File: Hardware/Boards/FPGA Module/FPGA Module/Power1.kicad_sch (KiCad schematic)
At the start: 0 parts

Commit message: FPGA Module schematic and part edits
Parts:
- added U2: LM7805MPX/NOPB, Package_TO_SOT_SMD:SOT-223-3_TabPin2, symbol DICE_FPGA_Module:LM7805MPX/NOPB
- added U3: AOZ2369QI-11, DICE_FPGA_Module:AOZ2369QI11, symbol DICE_FPGA_Module:AOZ2369QI-11
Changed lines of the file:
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@@
 	(generator "eeschema")
 	(generator_version "8.0")
-	(paper "A4")
+	(paper "A3")
 	(title_block
 		(title "Power1")
@@
 		(comment 1 "Designed by Michael Haahr")
 	)
+	(symbol
+		(lib_id "DICE_FPGA_Module:LM7805MPX/NOPB")
+		(at 63.5 118.11 0)
+		(unit 1)
+		(exclude_from_sim no)
+		(in_bom yes)
+		(on_board yes)
+		(dnp no)
+		(fields_autoplaced yes)
+		(property "Reference" "U2"
+			(at 63.5 109.22 0)
+			(effects
+				(font
+					(size 1.27 1.27)
+				)
+			)
+		)
+		(property "Value" "LM7805MPX/NOPB"
+			(at 63.5 111.76 0)
+			(effects
+				(font
+					(size 1.27 1.27)
+				)
+			)
+		)
+		(property "Footprint" "Package_TO_SOT_SMD:SOT-223-3_TabPin2"
+			(at 63.5 118.11 0)
+			(effects
+				(font
+					(size 1.27 1.27)
+				)
+				(hide yes)
+			)
+		)
+		(property "Datasheet" "https://ti.com/lit/ds/symlink/lm7800.pdf"
+			(at 63.5 118.11 0)
+			(effects
+				(font
+					(size 1.27 1.27)
+				)
+				(hide yes)
+			)
+		)
+		(property "Description" "Wide VIN 1.5-A 5V Regulator"
+			(at 63.5 118.11 0)
+			(effects
+				(font
+					(size 1.27 1.27)
+				)
+				(hide yes)
+			)
+		)
+		(pin "2"
+		)
+		(pin "3"
+		)
+		(pin "1"
+		)
+		(instances
+			(project ""
+				(path "/199f10e2-d4b4-4a27-9e84-7b1ce2ae6bf0/0c296310-f788-47f0-8a3f-43c3444563e8/e751a632-5f45-4f29-8d0a-1f9649251d32"
+					(reference "U2")
+					(unit 1)
+				)
+			)
+		)
+	)
+	(symbol
+		(lib_id "DICE_FPGA_Module:AOZ2369QI-11")
+		(at 63.5 63.5 0)
+		(unit 1)
+		(exclude_from_sim no)
+		(in_bom yes)
+		(on_board yes)
+		(dnp no)
+		(fields_autoplaced yes)
+		(property "Reference" "U3"
+			(at 63.5 27.94 0)
+			(effects
+				(font
+					(size 1.27 1.27)
+				)
+			)
+		)
+		(property "Value" "AOZ2369QI-11"
+			(at 63.5 30.48 0)
+			(effects
+				(font
+					(size 1.27 1.27)
+				)
+			)
+		)
+		(property "Footprint" "DICE_FPGA_Module:AOZ2369QI11"
+			(at 63.5 58.42 0)
+			(effects
+				(font
+					(size 1.27 1.27)
+				)
+				(hide yes)
+			)
+		)
+		(property "Datasheet" "https://www.aosmd.com/res/datasheets/AOZ2369QI-11.pdf"
+			(at 63.5 63.5 0)
+			(effects
+				(font
+					(size 1.27 1.27)
+				)
+				(hide yes)
+			)
+		)
+		(property "Description" "24V/30A Synchronous EZBuck Regulator"
+			(at 63.5 63.5 0)
+			(effects
+				(font
+					(size 1.27 1.27)
+				)
+				(hide yes)
+			)
+		)
+		(pin "14"
+		)
+		(pin "22"
+		)
+		(pin "25"
+		)
+		(pin "6"
+		)
+		(pin "7"
+		)
+		(pin "8"
+		)
+		(pin "11"
+		)
+		(pin "19"
+		)
+		(pin "5"
+		)
+		(pin "21"
+		)
+		(pin "18"
+		)
+		(pin "24"
+		)
+		(pin "27"
+		)
+		(pin "12"
+		)
+		(pin "13"
+		)
+		(pin "17"
+		)
+		(pin "15"
+		)
+		(pin "26"
+		)
+		(pin "28"
+		)
+		(pin "16"
+		)
+		(pin "3"
+		)
+		(pin "20"
+		)
+		(pin "23"
+		)
+		(pin "1"
+		)
+		(pin "10"
+		)
+		(pin "2"
+		)
+		(pin "4"
+		)
+		(pin "9"
+		)
+		(instances
+			(project ""
+				(path "/199f10e2-d4b4-4a27-9e84-7b1ce2ae6bf0/0c296310-f788-47f0-8a3f-43c3444563e8/e751a632-5f45-4f29-8d0a-1f9649251d32"
+					(reference "U3")
+					(unit 1)
+				)
+			)
+		)
+	)
 )

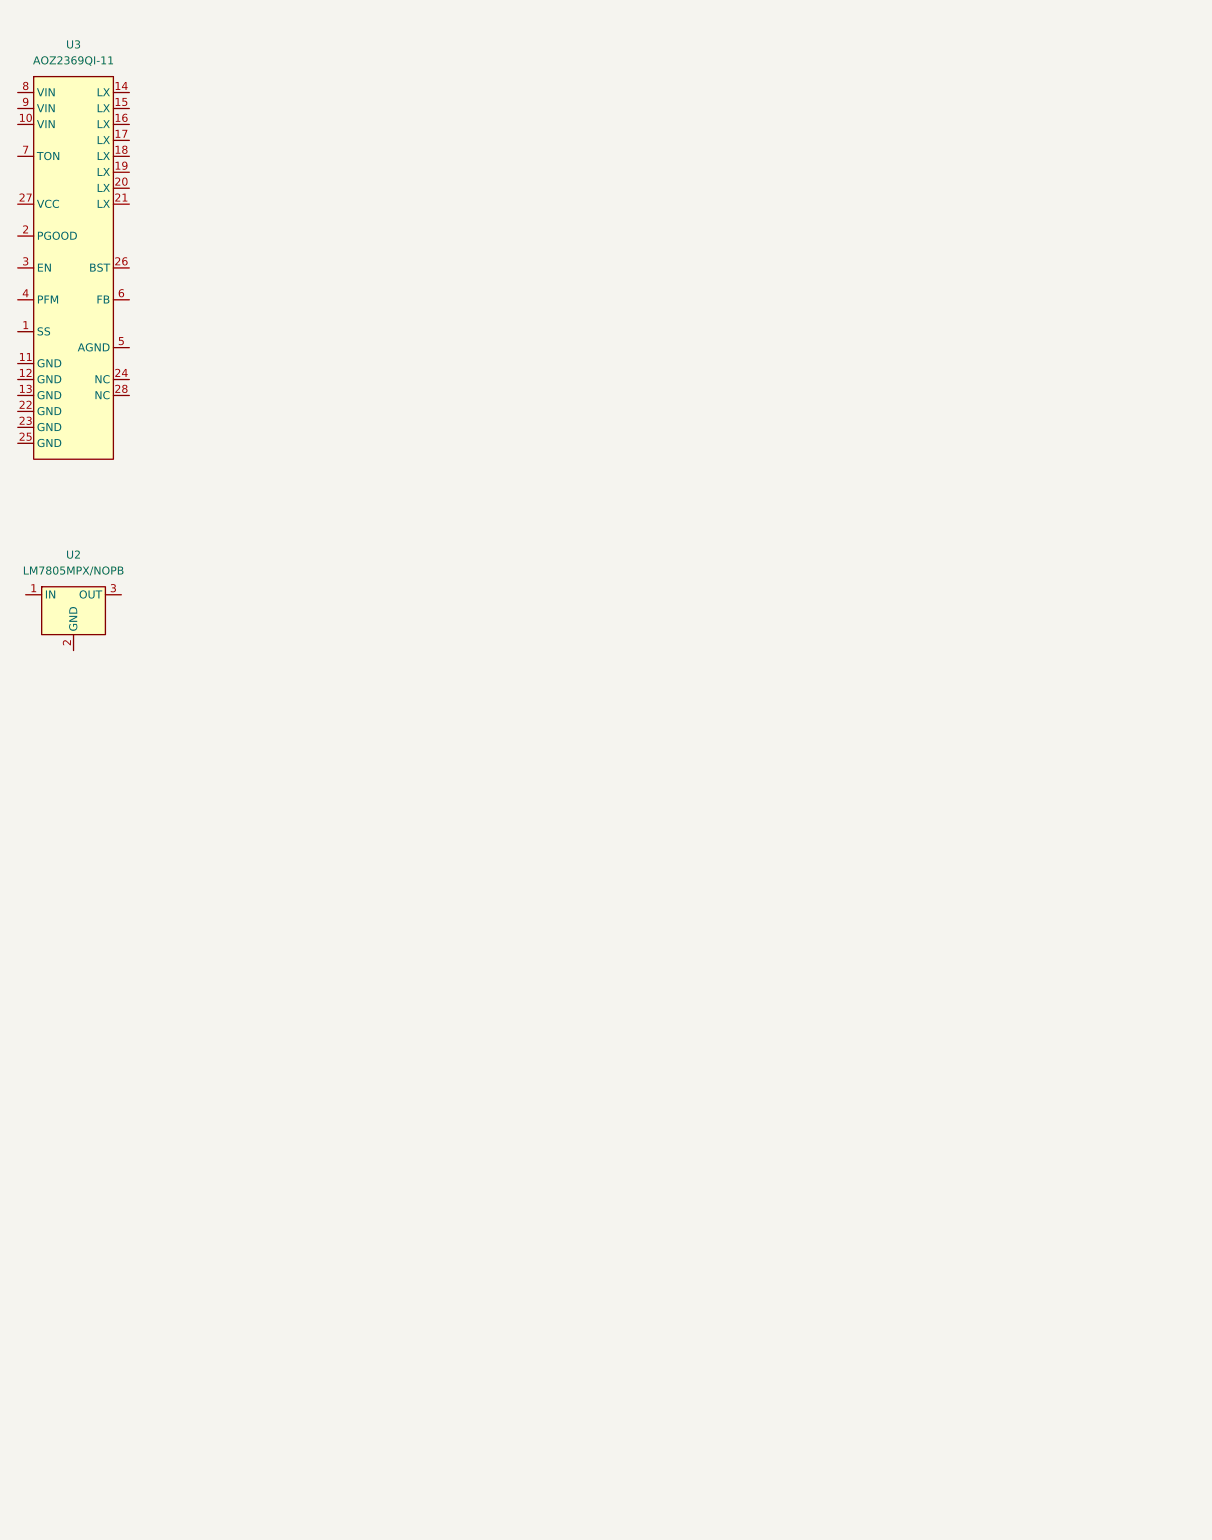
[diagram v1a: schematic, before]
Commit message: FPGA Board schematic work
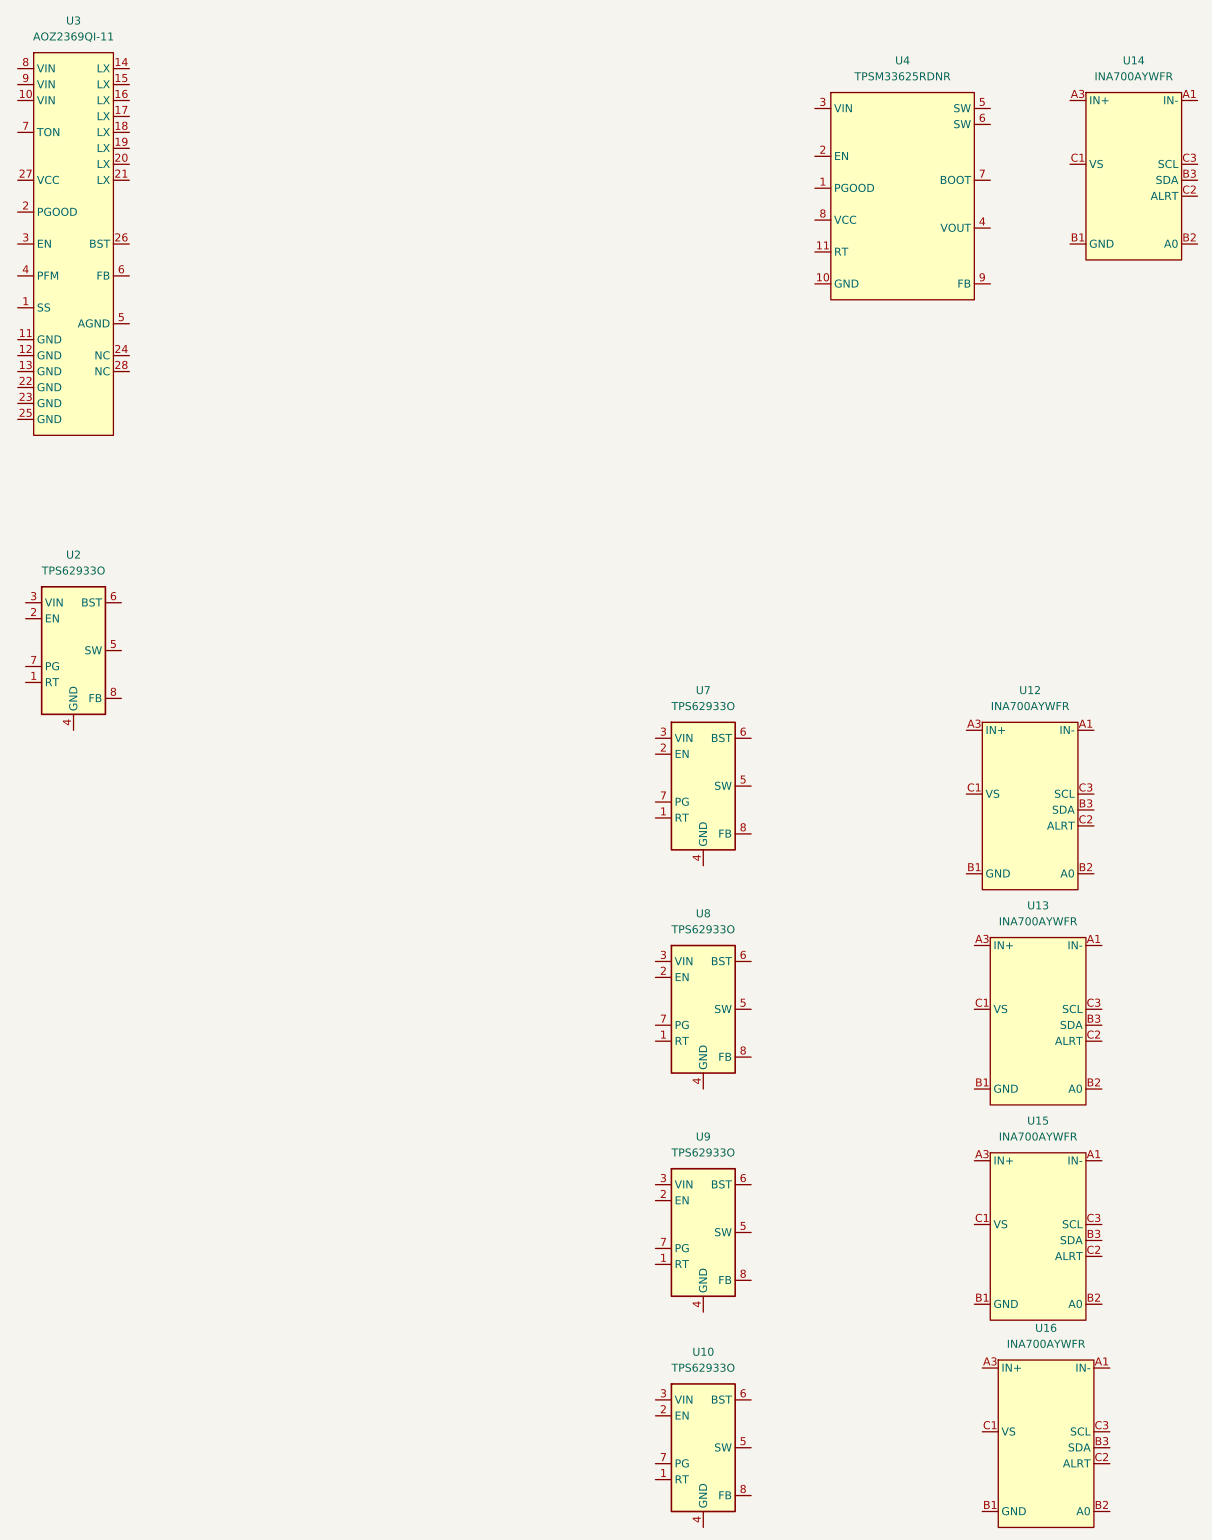
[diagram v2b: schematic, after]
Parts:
- removed U2: LM7805MPX/NOPB, Package_TO_SOT_SMD:SOT-223-3_TabPin2, symbol DICE_FPGA_Module:LM7805MPX/NOPB
- added U10, U2, U7, U8, U9: TPS62933O, Package_TO_SOT_SMD:SOT-583-8, symbol Regulator_Switching:TPS62933O
- added U12, U13, U14, U15, U16: INA700AYWFR, FPGA Module:INA700_AYWFR, symbol FPGA Module:INA700
- added U4: TPSM33625RDNR, FPGA Module:RDN0011A-MFG, symbol FPGA Module:TPSM33625
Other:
- moved on the sheet: U3

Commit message: FPGA Module Schematic work
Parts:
- removed U3: AOZ2369QI-11, DICE_FPGA_Module:AOZ2369QI11, symbol DICE_FPGA_Module:AOZ2369QI-11
- added C13, C17, C21, C23, C24: 100nF, Capacitor_SMD:C_0402_1005Metric, symbol Device:C_Small
- added C14, C15, C16: 100uF, Capacitor_SMD:C_0805_2012Metric, symbol Device:C_Small
- added C18: 4.7uF, Capacitor_SMD:C_0402_1005Metric, symbol Device:C_Small
- added C19, C20: 22uF, Capacitor_SMD:C_0805_2012Metric, symbol Device:C_Small
- added C22: 10uF, Capacitor_SMD:C_0603_1608Metric, symbol Device:C_Small
- added C25: 47uF, Capacitor_SMD:C_0603_1608Metric, symbol Device:C_Small
- added D2: LED, LED_SMD:LED_0603_1608Metric, symbol Device:LED
- added L1: 0.47uH, FPGA Module:INDM135125X500N, symbol Device:L
- added L2: 6.8uH, symbol Device:L
- added R10, R7, R8, R9: 3.3k, Resistor_SMD:R_0402_1005Metric, symbol Device:R_US
- added R11, R12: 33R, Resistor_SMD:R_0402_1005Metric, symbol Device:R_US
- added R13: 52.3k, Resistor_SMD:R_0402_1005Metric, symbol Device:R_US
- added R14: 9.09k, Resistor_SMD:R_0402_1005Metric, symbol Device:R_US
- added R15: 10k, Resistor_SMD:R_0402_1005Metric, symbol Device:R_US
- added R3: 100k, Resistor_SMD:R_0402_1005Metric, symbol Device:R_US
- added R4: 240k, Resistor_SMD:R_0402_1005Metric, symbol Device:R_US
- added R5: 67.3k, Resistor_SMD:R_0402_1005Metric, symbol Device:R_US
- added R6: 1mOhm, Resistor_SMD:R_1206_3216Metric, symbol Device:R_US
- added U18: INA236, Package_TO_SOT_SMD:SOT-23-8, symbol FPGA Module:INA236
- added U3: AOZ2369QI-11, FPGA Module:AOZ2369QI11, symbol FPGA Module:AOZ2369QI-11
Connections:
- net PP_VUSB: now reaches U2.3 (VIN)
- net PP_VUSB: now also C19.1, C20.1, C22.1, C23.1, R5.1, U3.10 (VIN), U3.8 (VIN), U3.9 (VIN)
- net GND: now reaches U2.4 (GND)
- net GND: now also C14.2, C15.2, C16.2, C17.2, C18.2, C19.2, C20.2, C21.2, C22.2, C23.2, C25.2, D2.1 (K), R15.2, R4.2, U18.3 (GND), U3.11 (GND), U3.12 (GND), U3.13 (GND), U3.22 (GND), U3.23 (GND), U3.25 (GND), U3.4 (PFM), U3.5 (AGND)
- net at U2.5 (SW): now also C24.2, L2.1
- net at U2.6 (BST): now also C24.1
- net at U2.8 (FB): now also R13.2, R15.1
- new net: R5.2, U3.7 (TON)
- new net: C17.1, U3.1 (SS)
- new net: C13.1, L1.1, U3.14 (LX), U3.15 (LX), U3.16 (LX), U3.17 (LX), U3.18 (LX), U3.19 (LX), U3.20 (LX), U3.21 (LX)
- new net: C13.2, U3.26 (BST)
- new net: C25.1, L2.2, R13.1
- new net +0V85: R6.2, U18.2 (IN-)
- new net +3V3_AO: C21.1, R10.1, R7.1, R8.1, R9.1, U18.4 (VS)
- new net +5V0_AO: C18.1, U3.27 (VCC)
- new net 0V85_EN: U3.3 (EN)
- new net 0V85_FB: R3.2, R4.1, U3.6 (FB)
- new net 0V85_ISNS_ALERT: R8.2, U18.8 (ALERT)
- new net 0V85_ISNS_I2C0_SCL: R11.1, U18.5 (SCL)
- new net 0V85_ISNS_I2C0_SDA: R12.1, U18.6 (SDA)
- new net 0V85_PGOOD: D2.2 (A), R7.2, U3.2 (PGOOD)
- new net 0V85_R: C14.1, C15.1, C16.1, L1.2, R3.1, R6.1, U18.1 (IN+)
- new net I2C0_SCL: R11.2, R9.2
- new net I2C0_SDA: R10.2, R12.2
- no-connect marks 0 -> 2
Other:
- note added: "0.85V FPGA Core Voltage + Current Sense"
- moved on the sheet: U14, U2, U4

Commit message: FPGA Module Power Schematic Changes
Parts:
- added C26: 4.7uF, Capacitor_SMD:C_0402_1005Metric, symbol Device:C_Small
- added C27: 10nF, Capacitor_SMD:C_0402_1005Metric, symbol Device:C_Small
- added C42, C49: 10uF, Capacitor_SMD:C_0603_1608Metric, symbol Device:C_Small
- added C43, C44, C48, C50, C51, C54: 100nF, Capacitor_SMD:C_0402_1005Metric, symbol Device:C_Small
- added C45, C46, C47: 47uF, Capacitor_SMD:C_0603_1608Metric, symbol Device:C_Small
- added C52, C53: 100uF, Capacitor_SMD:C_0805_2012Metric, symbol Device:C_Small
- added D3, D4, D6, D7: LED, LED_SMD:LED_0603_1608Metric, symbol Device:LED
- added D5: 3V3_AO ON, LED_SMD:LED_0603_1608Metric, symbol Device:LED
- added L3: 1.5uH, FPGA Module:SRU1038100Y, symbol Device:L
- added L4: 2.2uH, FPGA Module:SRU10382R2Y, symbol Device:L
- added R16, R26, R27, R28, R34, R35, R41: 3.3k, Resistor_SMD:R_0402_1005Metric, symbol Device:R_US
- added R17: 30.9k, Resistor_SMD:R_0402_1005Metric, symbol Device:R_US
- added R25, R31, R38: 10k, Resistor_SMD:R_0402_1005Metric, symbol Device:R_US
- added R29: 9.76k, Resistor_SMD:R_0402_1005Metric, symbol Device:R_US
- added R30: 1.24k, Resistor_SMD:R_0402_1005Metric, symbol Device:R_US
- added R32, R33, R39, R40: 33R, Resistor_SMD:R_0402_1005Metric, symbol Device:R_US
- added R36: 9.09k, Resistor_SMD:R_0402_1005Metric, symbol Device:R_US
- added R37: 4.99k, Resistor_SMD:R_0402_1005Metric, symbol Device:R_US
- added U19: TPS74801AWDRC, Package_SON:VSON-10-1EP_3x3mm_P0.5mm_EP1.65x2.4mm_ThermalVias, symbol Regulator_Linear:TPS74801AWDRC
- L2: footprint (none) -> FPGA Module:THMC0503SP-6R8MG-D; MPN (none) -> THMC0503SP-6R8MG-D
- R14: now not fitted
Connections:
- net +3V3_AO: now also U12.C1 (VS), U13.C1 (VS), C48.1, C54.1, D5.2 (A), R16.1, R17.1, R26.2, R28.1, R34.1, R35.1, R41.1, U19.10 (OUT), U19.9 (OUT)
- net +5V0_AO: now also C25.1, L2.2, R13.1, C26.1, U19.1 (IN), U19.2 (IN), U19.4 (BIAS), U19.5 (EN)
- net 0V85_PGOOD: now also D2.1 (K); no longer D2.2 (A), R7.2
- net GND: now also R14.2, U12.B1 (GND), U13.B1 (GND), U7.4 (GND), U8.4 (GND), C26.2, C27.2, C42.2, C43.2, C45.2, C46.2, C47.2, C48.2, C49.2, C50.2, C52.2, C53.2, C54.2, R25.2, R27.2, R29.2, R31.2, R36.2, R38.2, U19.11 (GND), U19.6 (GND); no longer D2.1 (K)
- net I2C0_SCL: now also R32.2, R39.2
- net I2C0_SDA: now also R33.2, R40.2
- net PP_VUSB: now also U2.2 (EN), U7.2 (EN), U7.3 (VIN), U8.2 (EN), U8.3 (VIN), C42.1, C43.1, C49.1, C50.1
- net +0V9M: now reaches U12.A1 (IN-)
- net +0V9M_R: now reaches U12.A3 (IN+)
- net +0V9M_R: now also C45.1, C46.1, C47.1, L3.2, R30.1
- net 0V9_ISNS_I2C0_SDA: now reaches U12.B3 (SDA)
- net 0V9_ISNS_I2C0_SDA: now also R33.1
- net 0V9_ISNS_ALERT: now reaches U12.C2 (ALRT)
- net 0V9_ISNS_ALERT: now also R34.2
- net 0V9_ISNS_I2C0_SCL: now reaches U12.C3 (SCL)
- net 0V9_ISNS_I2C0_SCL: now also R32.1
- net +1V2M: now reaches U13.A1 (IN-)
- net 1V2M_R: now reaches U13.A3 (IN+)
- net 1V2M_R: now also C52.1, C53.1, L4.2, R37.1
- net 1V2M_ISNS_I2C0_SDA: now reaches U13.B3 (SDA)
- net 1V2M_ISNS_I2C0_SDA: now also R40.1
- net 1V2M_ISNS_ALERT: now reaches U13.C2 (ALRT)
- net 1V2M_ISNS_ALERT: now also R41.2
- net 1V2M_ISNS_I2C0_SCL: now reaches U13.C3 (SCL)
- net 1V2M_ISNS_I2C0_SCL: now also R39.1
- net at R14.1: now also U2.1 (RT)
- net 5V0_AO_PGOOD: now reaches U2.7 (PG)
- net 5V0_AO_PGOOD: now also D3.1 (K)
- net 5V0_AO_FB: now reaches R13.2, R15.1, U2.8 (FB)
- net at U8.1 (RT): now also R36.1
- net at U8.5 (SW): now also C51.2, L4.1
- net at U8.6 (BST): now also C51.1
- net 1V2M_PGOOD: now reaches U8.7 (PG)
- net 1V2M_PGOOD: now also D7.1 (K)
- net 1V2M_FB: now reaches U8.8 (FB)
- net 1V2M_FB: now also R37.2, R38.1
- net at U7.1 (RT): now also R29.1
- net at U7.5 (SW): now also C44.2, L3.1
- net at U7.6 (BST): now also C44.1
- net 0V9_PGOOD: now reaches U7.7 (PG)
- net 0V9_PGOOD: now also D6.1 (K)
- net 0V9_FB: now reaches U7.8 (FB)
- net 0V9_FB: now also R30.2, R31.1
- new net: D5.1 (K), R27.1
- new net: D7.2 (A), R35.2
- new net: D3.2 (A), R16.2
- new net: D4.1 (K), U19.3 (PG)
- new net: C27.1, U19.7 (SS)
- new net: D2.2 (A), R7.2
- new net: D6.2 (A), R28.2
- new net: D4.2 (A), R26.1
- new net 3V3_AO_FB: R17.2, R25.1, U19.8 (FB)
- no-connect marks 2 -> 5
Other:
- note added: "0.9V MGTAVCC"
- note added: "3.3V Always On"
- note added: "5.0V Always On"
- moved on the sheet: C22, C23, C24, C25, D2, L2, R13, R15, R7, U10, U12, U13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
